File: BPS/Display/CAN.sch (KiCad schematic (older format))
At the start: 23 parts, among them J5 CAN_Out, U4 CDSOT23-T24CAN, U5 ADM3055E

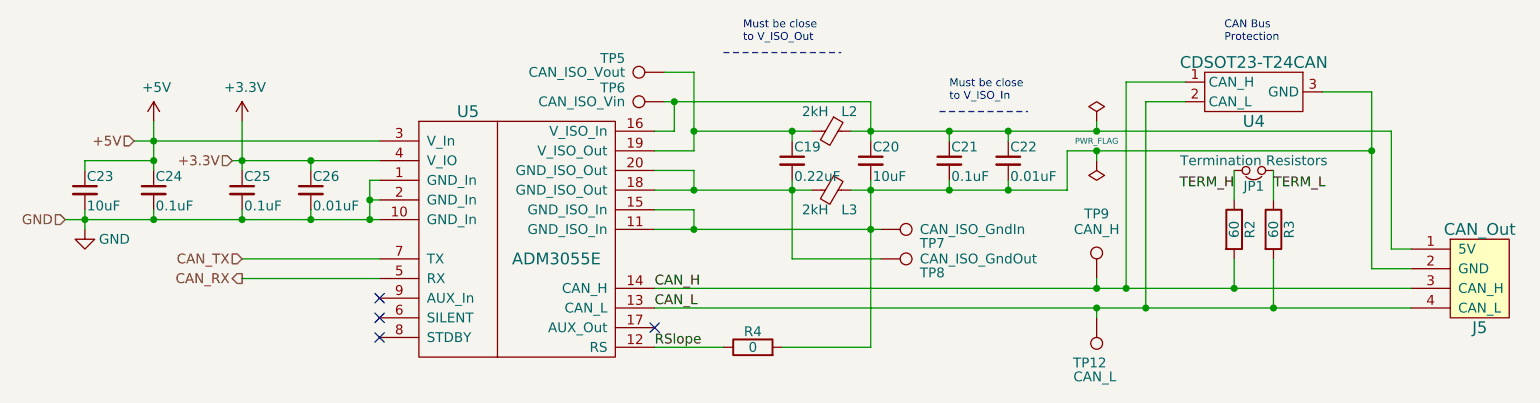
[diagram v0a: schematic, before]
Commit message: Creates schematics for display.
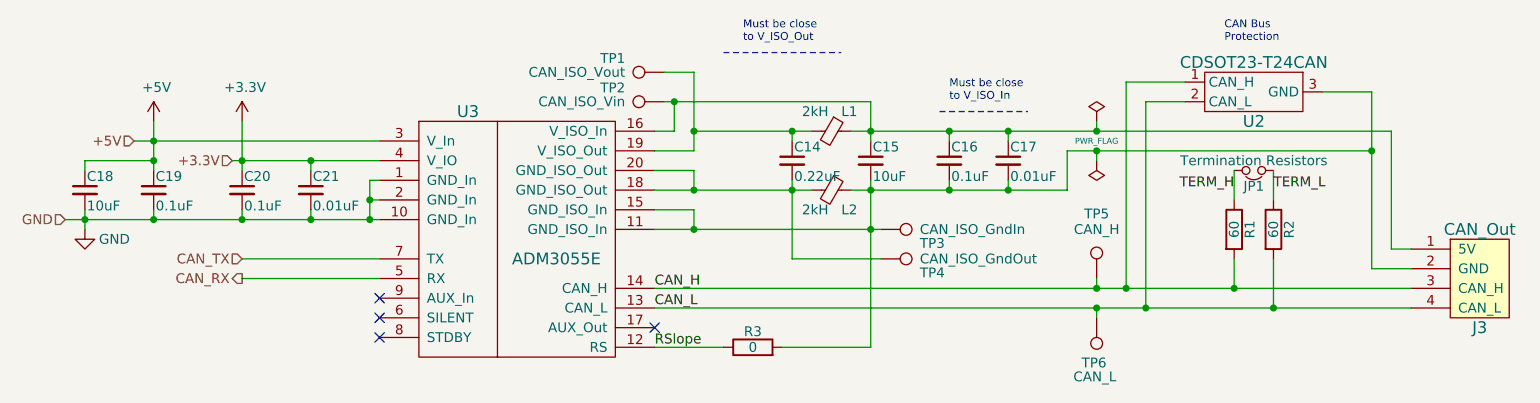
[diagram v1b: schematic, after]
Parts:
- renumbered C19 to C14, C20 to C15, C21 to C16, C22 to C17, C23 to C18, C24 to C19, C25 to C20, C26 to C21, J5 to J3, L2 to L1, L3 to L2, R2 to R1, R3 to R2, R4 to R3, TP5 to TP1, TP6 to TP2, TP7 to TP3, TP8 to TP4, TP9 to TP5, TP12 to TP6, U4 to U2, U5 to U3
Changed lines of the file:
@@
 EESchema Schematic File Version 4
-LIBS:BPSMaster-cache
+LIBS:BPSDisplay-cache
 EELAYER 29 0
 EELAYER END
 $Descr A4 11693 8268
 encoding utf-8
-Sheet 3 7
+Sheet 2 3
 Title ""
 Date ""
@@
 $EndDescr
 $Comp
-L utsvt-connectors:CANConnector J5
+L utsvt-connectors:CANConnector J3
 U 1 1 5C2B42F3
 P 9250 3800
-F 0 "J5" H 9250 3550 60  0000 C CNN
+F 0 "J3" H 9250 3550 60  0000 C CNN
 F 1 "CAN_Out" H 9250 4050 60  0000 C CNN
 F 2 "UTSVT_Connectors:Molex_MicroFit3.0_1x4xP3.00mm_PolarizingPeg_Vertical" H 9400 4100 60  0001 C CNN
@@
 $EndComp
 $Comp
-L Device:R R3
+L Device:R R2
 U 1 1 5C2B42FA
 P 8200 3550
-F 0 "R3" V 8280 3550 50  0000 C CNN
+F 0 "R2" V 8280 3550 50  0000 C CNN
 F 1 "60" V 8200 3550 50  0000 C CNN
 F 2 "Resistor_SMD:R_0805_2012Metric" V 8130 3550 50  0001 C CNN
@@
 $EndComp
 $Comp
-L Device:R R2
+L Device:R R1
 U 1 1 5C2B4301
 P 8000 3550
-F 0 "R2" V 8080 3550 50  0000 C CNN
+F 0 "R1" V 8080 3550 50  0000 C CNN
 F 1 "60" V 8000 3550 50  0000 C CNN
 F 2 "Resistor_SMD:R_0805_2012Metric" V 7930 3550 50  0001 C CNN
@@
 $EndComp
 $Comp
-L Device:C_Small C23
+L Device:C_Small C18
 U 1 1 5C2B4310
 P 2150 3350
-F 0 "C23" H 2160 3420 50  0000 L CNN
+F 0 "C18" H 2160 3420 50  0000 L CNN
 F 1 "10uF" H 2160 3270 50  0000 L CNN
 F 2 "Capacitor_SMD:C_0805_2012Metric" H 2150 3350 50  0001 C CNN
@@
 $EndComp
 $Comp
-L Device:C_Small C24
+L Device:C_Small C19
 U 1 1 5C2B4317
 P 2500 3350
-F 0 "C24" H 2510 3420 50  0000 L CNN
+F 0 "C19" H 2510 3420 50  0000 L CNN
 F 1 "0.1uF" H 2510 3270 50  0000 L CNN
 F 2 "Capacitor_SMD:C_0805_2012Metric" H 2500 3350 50  0001 C CNN
@@
 $EndComp
 $Comp
-L Device:C_Small C25
+L Device:C_Small C20
 U 1 1 5C2B431E
 P 2950 3350
-F 0 "C25" H 2960 3420 50  0000 L CNN
+F 0 "C20" H 2960 3420 50  0000 L CNN
 F 1 "0.1uF" H 2960 3270 50  0000 L CNN
 F 2 "Capacitor_SMD:C_0805_2012Metric" H 2950 3350 50  0001 C CNN
@@
 $EndComp
 $Comp
-L Device:C_Small C26
+L Device:C_Small C21
 U 1 1 5C2B4325
 P 3300 3350
-F 0 "C26" H 3310 3420 50  0000 L CNN
+F 0 "C21" H 3310 3420 50  0000 L CNN
 F 1 "0.01uF" H 3310 3270 50  0000 L CNN
 F 2 "Capacitor_SMD:C_0805_2012Metric" H 3300 3350 50  0001 C CNN
@@
 $EndComp
 $Comp
-L Device:C_Small C20
+L Device:C_Small C15
 U 1 1 5C2B432E
 P 6150 3200
-F 0 "C20" H 6160 3270 50  0000 L CNN
+F 0 "C15" H 6160 3270 50  0000 L CNN
 F 1 "10uF" H 6160 3120 50  0000 L CNN
 F 2 "Capacitor_SMD:C_0805_2012Metric" H 6150 3200 50  0001 C CNN
@@
 $EndComp
 $Comp
-L Device:C_Small C19
+L Device:C_Small C14
 U 1 1 5C2B4335
 P 5750 3200
-F 0 "C19" H 5760 3270 50  0000 L CNN
+F 0 "C14" H 5760 3270 50  0000 L CNN
 F 1 "0.22uF" H 5760 3120 50  0000 L CNN
 F 2 "Capacitor_SMD:C_0805_2012Metric" H 5750 3200 50  0001 C CNN
@@
 $EndComp
 $Comp
-L Device:Ferrite_Bead_Small L2
+L Device:Ferrite_Bead_Small L1
 U 1 1 5C2B433C
 P 5950 3050
-F 0 "L2" V 5850 3100 50  0000 L CNN
+F 0 "L1" V 5850 3100 50  0000 L CNN
 F 1 "2kH" V 5850 2900 50  0000 L CNN
 F 2 "Inductor_SMD:L_0805_2012Metric" V 5880 3050 50  0001 C CNN
@@
 $EndComp
 $Comp
-L Device:Ferrite_Bead_Small L3
+L Device:Ferrite_Bead_Small L2
 U 1 1 5C2B4343
 P 5950 3350
-F 0 "L3" V 6050 3400 50  0000 L CNN
+F 0 "L2" V 6050 3400 50  0000 L CNN
 F 1 "2kH" V 6050 3200 50  0000 L CNN
 F 2 "Inductor_SMD:L_0805_2012Metric" V 5880 3350 50  0001 C CNN
@@
 $EndComp
 $Comp
-L Device:C_Small C21
+L Device:C_Small C16
 U 1 1 5C2B434A
 P 6550 3200
-F 0 "C21" H 6560 3270 50  0000 L CNN
+F 0 "C16" H 6560 3270 50  0000 L CNN
 F 1 "0.1uF" H 6560 3120 50  0000 L CNN
 F 2 "Capacitor_SMD:C_0805_2012Metric" H 6550 3200 50  0001 C CNN
@@
 $EndComp
 $Comp
-L Device:C_Small C22
+L Device:C_Small C17
 U 1 1 5C2B4351
 P 6850 3200
-F 0 "C22" H 6860 3270 50  0000 L CNN
+F 0 "C17" H 6860 3270 50  0000 L CNN
 F 1 "0.01uF" H 6860 3120 50  0000 L CNN
 F 2 "Capacitor_SMD:C_0805_2012Metric" H 6850 3200 50  0001 C CNN
@@
 $EndComp
 $Comp
-L utsvt-chips:ADM3055E U5
+L utsvt-chips:ADM3055E U3
 U 1 1 5C2B4359
 P 4350 3600
-F 0 "U5" H 4100 4250 60  0000 C CNN
+F 0 "U3" H 4100 4250 60  0000 C CNN
 F 1 "ADM3055E" H 4550 3500 60  0000 C CNN
 F 2 "UTSVT_ICs:SOIC-20W_7.5x15.4mm_Pitch1.27mm" H 4350 3700 60  0001 C CNN
@@
 Must be close\nto V_ISO_In
 $Comp
-L Connector:TestPoint TP6
+L Connector:TestPoint TP2
 U 1 1 5C2B4371
 P 5100 2900
-F 0 "TP6" V 5200 3100 50  0000 L BNN
+F 0 "TP2" V 5200 3100 50  0000 L BNN
 F 1 "CAN_ISO_Vin" V 5100 3100 50  0000 L CNN
 F 2 "TestPoint:TestPoint_Keystone_5005-5009_Compact" H 5100 2900 50  0001 C CNN
@@
 $EndComp
 $Comp
-L Connector:TestPoint TP8
+L Connector:TestPoint TP4
 U 1 1 5C2B4378
 P 6200 3700
-F 0 "TP8" V 6300 3900 50  0000 L BNN
+F 0 "TP4" V 6300 3900 50  0000 L BNN
 F 1 "CAN_ISO_GndOut" V 6200 3900 50  0000 L CNN
 F 2 "TestPoint:TestPoint_Keystone_5005-5009_Compact" H 6200 3700 50  0001 C CNN
@@
 $EndComp
 $Comp
-L Connector:TestPoint TP7
+L Connector:TestPoint TP3
 U 1 1 5C2B437F
 P 6200 3550
-F 0 "TP7" V 6300 3750 50  0000 L BNN
+F 0 "TP3" V 6300 3750 50  0000 L BNN
 F 1 "CAN_ISO_GndIn" V 6200 3750 50  0000 L CNN
 F 2 "TestPoint:TestPoint_Keystone_5005-5009_Compact" H 6200 3550 50  0001 C CNN
@@
 $EndComp
 $Comp
-L Connector:TestPoint TP5
+L Connector:TestPoint TP1
 U 1 1 5C2B4386
 P 5100 2750
-F 0 "TP5" V 5200 2950 50  0000 L BNN
+F 0 "TP1" V 5200 2950 50  0000 L BNN
 F 1 "CAN_ISO_Vout" V 5100 2950 50  0000 L CNN
 F 2 "TestPoint:TestPoint_Keystone_5005-5009_Compact" H 5100 2750 50  0001 C CNN
@@
 NoConn ~ 3650 4100
 $Comp
-L power:PWR_FLAG #FLG03
+L power:PWR_FLAG #FLG0101
 U 1 1 5C2B4394
 P 7300 3000
-F 0 "#FLG03" H 7300 3075 50  0001 C CNN
+F 0 "#FLG0101" H 7300 3075 50  0001 C CNN
 F 1 "PWR_FLAG" H 7300 2900 30  0000 C CNN
 F 2 "" H 7300 3000 50  0001 C CNN
@@
 $EndComp
 $Comp
-L power:PWR_FLAG #FLG04
+L power:PWR_FLAG #FLG0102
 U 1 1 5C2B439A
 P 7300 3200
-F 0 "#FLG04" H 7300 3275 50  0001 C CNN
+F 0 "#FLG0102" H 7300 3275 50  0001 C CNN
 F 1 "PWR_FLAG" H 7200 3150 50  0001 L CNN
 F 2 "" H 7300 3200 50  0001 C CNN
@@
 $EndComp
 $Comp
-L utsvt-chips:CDSOT23-T24CAN U4
+L utsvt-chips:CDSOT23-T24CAN U2
 U 1 1 5C2B43A0
 P 8100 2850
-F 0 "U4" H 8100 2700 60  0000 C CNN
+F 0 "U2" H 8100 2700 60  0000 C CNN
 F 1 "CDSOT23-T24CAN" H 8100 3000 60  0000 C CNN
 F 2 "Package_TO_SOT_SMD:SOT-23W" H 8100 2850 60  0001 C CNN
@@
 CAN Bus\nProtection
 $Comp
-L Connector:TestPoint TP9
+L Connector:TestPoint TP5
 U 1 1 5C2B43B6
 P 7300 3800
-F 0 "TP9" H 7300 4100 50  0000 C BNN
+F 0 "TP5" H 7300 4100 50  0000 C BNN
 F 1 "CAN_H" H 7300 4050 50  0000 C CNN
 F 2 "TestPoint:TestPoint_Keystone_5005-5009_Compact" H 7300 3800 50  0001 C CNN
@@
 $EndComp
 $Comp
-L Connector:TestPoint TP12
+L Connector:TestPoint TP6
 U 1 1 5C2B43BD
 P 7300 4000
-F 0 "TP12" H 7250 4200 50  0000 L BNN
+F 0 "TP6" H 7250 4200 50  0000 L BNN
 F 1 "CAN_L" H 7200 4300 50  0000 L CNN
 F 2 "TestPoint:TestPoint_Keystone_5005-5009_Compact" H 7300 4000 50  0001 C CNN
@@
 $EndComp
 $Comp
-L Device:R R4
+L Device:R R3
 U 1 1 5C2B43C4
 P 5550 4150
-F 0 "R4" V 5630 4150 50  0000 C CNN
+F 0 "R3" V 5630 4150 50  0000 C CNN
 F 1 "0" V 5550 4150 50  0000 C CNN
 F 2 "Resistor_SMD:R_0805_2012Metric" V 5480 4150 50  0001 C CNN
@@
 	6150 3550 6200 3550
 $Comp
-L power:GND #PWR042
+L power:GND #PWR0118
 U 1 1 5C28BDDE
 P 2150 3550
-F 0 "#PWR042" H 2150 3300 50  0001 C CNN
+F 0 "#PWR0118" H 2150 3300 50  0001 C CNN
 F 1 "GND" H 2300 3500 50  0000 C CNN
 F 2 "" H 2150 3550 50  0001 C CNN
@@
 	2500 3000 2500 3100
 $Comp
-L power:+3.3V #PWR0133
+L power:+3.3V #PWR0119
 U 1 1 5C4ABE05
 P 2950 3000
-F 0 "#PWR0133" H 2950 2850 50  0001 C CNN
+F 0 "#PWR0119" H 2950 2850 50  0001 C CNN
 F 1 "+3.3V" H 2965 3173 50  0000 C CNN
 F 2 "" H 2950 3000 50  0001 C CNN
@@
 	2950 3000 2950 3200
 $Comp
-L power:+5V #PWR0132
+L power:+5V #PWR0120
 U 1 1 5C4C2AB0
 P 2500 3000
-F 0 "#PWR0132" H 2500 2850 50  0001 C CNN
+F 0 "#PWR0120" H 2500 2850 50  0001 C CNN
 F 1 "+5V" H 2515 3173 50  0000 C CNN
 F 2 "" H 2500 3000 50  0001 C CNN

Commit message: Display, Board Layout
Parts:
- J3: footprint UTSVT_Connectors:Molex_MicroFit3.0_1x4xP3.00mm_PolarizingPeg_Vertical -> Connector_Molex:Molex_Micro-Fit_3.0_43650-0400_1x04_P3.00mm_Horizontal; symbol utsvt-connectors:CANConnector -> BPSDisplay-rescue:CANConnector-utsvt-connectors
- U2: symbol utsvt-chips:CDSOT23-T24CAN -> BPSDisplay-rescue:CDSOT23-T24CAN-utsvt-chips
- U3: symbol utsvt-chips:ADM3055E -> BPSDisplay-rescue:ADM3055E-utsvt-chips
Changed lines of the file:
@@
 $EndDescr
 $Comp
-L utsvt-connectors:CANConnector J3
+L BPSDisplay-rescue:CANConnector-utsvt-connectors J3
 U 1 1 5C2B42F3
 P 9250 3800
 F 0 "J3" H 9250 3550 60  0000 C CNN
 F 1 "CAN_Out" H 9250 4050 60  0000 C CNN
-F 2 "UTSVT_Connectors:Molex_MicroFit3.0_1x4xP3.00mm_PolarizingPeg_Vertical" H 9400 4100 60  0001 C CNN
+F 2 "Connector_Molex:Molex_Micro-Fit_3.0_43650-0400_1x04_P3.00mm_Horizontal" H 9400 4100 60  0001 C CNN
 F 3 "" H 9400 4100 60  0001 C CNN
 	1    9250 3800
@@
 $EndComp
 $Comp
-L utsvt-chips:ADM3055E U3
+L BPSDisplay-rescue:ADM3055E-utsvt-chips U3
 U 1 1 5C2B4359
 P 4350 3600
@@
 $EndComp
 $Comp
-L utsvt-chips:CDSOT23-T24CAN U2
+L BPSDisplay-rescue:CDSOT23-T24CAN-utsvt-chips U2
 U 1 1 5C2B43A0
 P 8100 2850

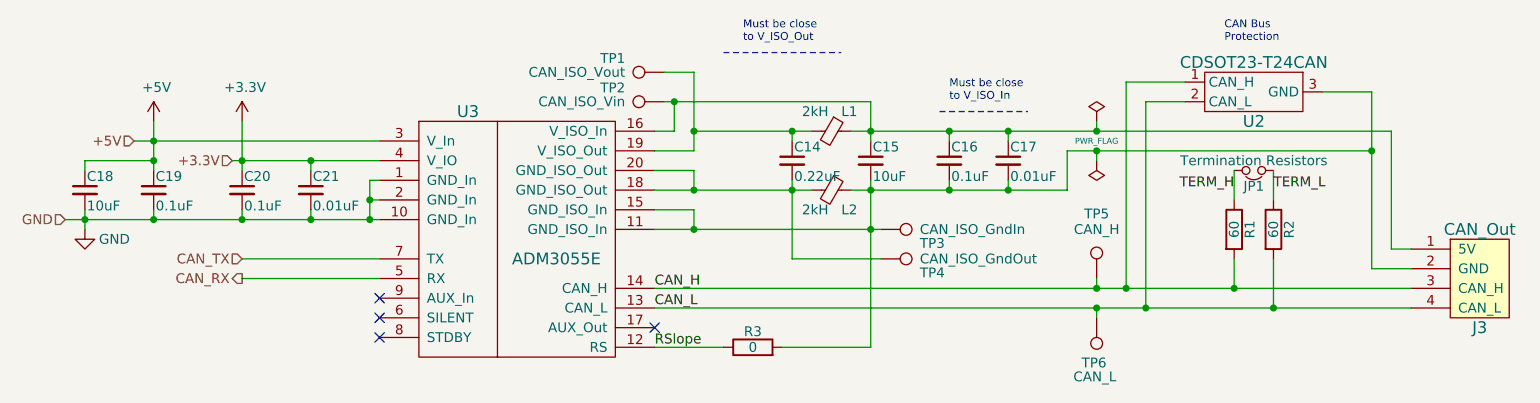
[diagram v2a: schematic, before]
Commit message: Adds display board
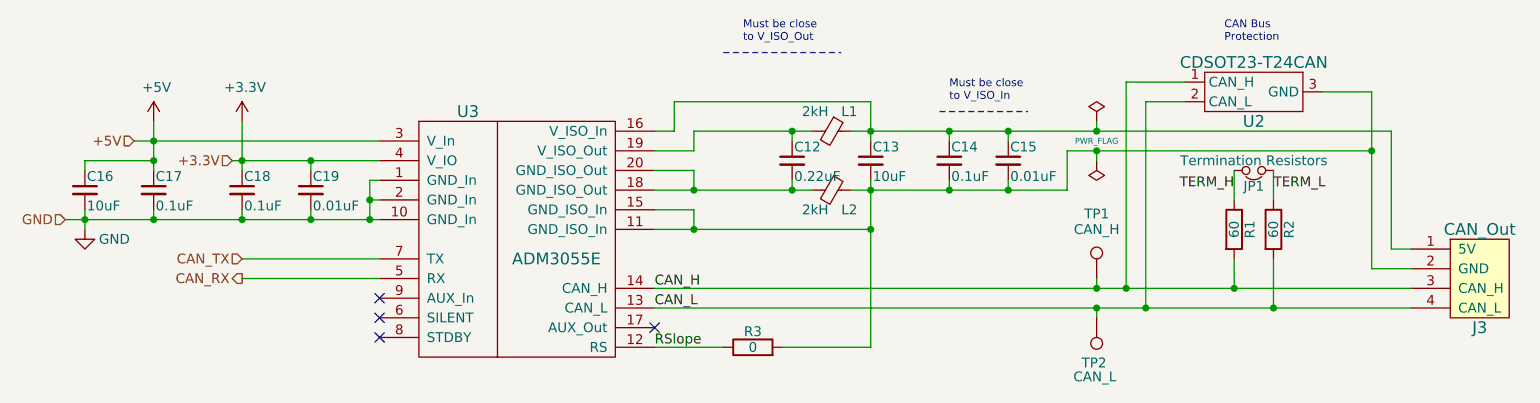
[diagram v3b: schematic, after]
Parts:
- removed TP1: CAN_ISO_Vout, TestPoint:TestPoint_Keystone_5005-5009_Compact, symbol Connector:TestPoint
- removed TP2: CAN_ISO_Vin, TestPoint:TestPoint_Keystone_5005-5009_Compact, symbol Connector:TestPoint
- removed TP3: CAN_ISO_GndIn, TestPoint:TestPoint_Keystone_5005-5009_Compact, symbol Connector:TestPoint
- removed TP4: CAN_ISO_GndOut, TestPoint:TestPoint_Keystone_5005-5009_Compact, symbol Connector:TestPoint
- renumbered C14 to C12, C15 to C13, C16 to C14, C17 to C15, C18 to C16, C19 to C17, C20 to C18, C21 to C19, TP5 to TP1, TP6 to TP2
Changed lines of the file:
@@
 EESchema Schematic File Version 4
-LIBS:BPSDisplay-cache
-EELAYER 29 0
+EELAYER 30 0
 EELAYER END
 $Descr A4 11693 8268
 encoding utf-8
-Sheet 2 3
+Sheet 2 4
 Title ""
 Date ""
@@
 $EndComp
 $Comp
-L Device:C_Small C18
+L Device:C_Small C16
 U 1 1 5C2B4310
 P 2150 3350
-F 0 "C18" H 2160 3420 50  0000 L CNN
+F 0 "C16" H 2160 3420 50  0000 L CNN
 F 1 "10uF" H 2160 3270 50  0000 L CNN
 F 2 "Capacitor_SMD:C_0805_2012Metric" H 2150 3350 50  0001 C CNN
@@
 $EndComp
 $Comp
-L Device:C_Small C19
+L Device:C_Small C17
 U 1 1 5C2B4317
 P 2500 3350
-F 0 "C19" H 2510 3420 50  0000 L CNN
+F 0 "C17" H 2510 3420 50  0000 L CNN
 F 1 "0.1uF" H 2510 3270 50  0000 L CNN
 F 2 "Capacitor_SMD:C_0805_2012Metric" H 2500 3350 50  0001 C CNN
@@
 $EndComp
 $Comp
-L Device:C_Small C20
+L Device:C_Small C18
 U 1 1 5C2B431E
 P 2950 3350
-F 0 "C20" H 2960 3420 50  0000 L CNN
+F 0 "C18" H 2960 3420 50  0000 L CNN
 F 1 "0.1uF" H 2960 3270 50  0000 L CNN
 F 2 "Capacitor_SMD:C_0805_2012Metric" H 2950 3350 50  0001 C CNN
@@
 $EndComp
 $Comp
-L Device:C_Small C21
+L Device:C_Small C19
 U 1 1 5C2B4325
 P 3300 3350
-F 0 "C21" H 3310 3420 50  0000 L CNN
+F 0 "C19" H 3310 3420 50  0000 L CNN
 F 1 "0.01uF" H 3310 3270 50  0000 L CNN
 F 2 "Capacitor_SMD:C_0805_2012Metric" H 3300 3350 50  0001 C CNN
@@
 $EndComp
 $Comp
-L Device:C_Small C15
+L Device:C_Small C13
 U 1 1 5C2B432E
 P 6150 3200
-F 0 "C15" H 6160 3270 50  0000 L CNN
+F 0 "C13" H 6160 3270 50  0000 L CNN
 F 1 "10uF" H 6160 3120 50  0000 L CNN
 F 2 "Capacitor_SMD:C_0805_2012Metric" H 6150 3200 50  0001 C CNN
@@
 $EndComp
 $Comp
-L Device:C_Small C14
+L Device:C_Small C12
 U 1 1 5C2B4335
 P 5750 3200
-F 0 "C14" H 5760 3270 50  0000 L CNN
+F 0 "C12" H 5760 3270 50  0000 L CNN
 F 1 "0.22uF" H 5760 3120 50  0000 L CNN
 F 2 "Capacitor_SMD:C_0805_2012Metric" H 5750 3200 50  0001 C CNN
@@
 $EndComp
 $Comp
-L Device:C_Small C16
+L Device:C_Small C14
 U 1 1 5C2B434A
 P 6550 3200
-F 0 "C16" H 6560 3270 50  0000 L CNN
+F 0 "C14" H 6560 3270 50  0000 L CNN
 F 1 "0.1uF" H 6560 3120 50  0000 L CNN
 F 2 "Capacitor_SMD:C_0805_2012Metric" H 6550 3200 50  0001 C CNN
@@
 $EndComp
 $Comp
-L Device:C_Small C17
+L Device:C_Small C15
 U 1 1 5C2B4351
 P 6850 3200
-F 0 "C17" H 6860 3270 50  0000 L CNN
+F 0 "C15" H 6860 3270 50  0000 L CNN
 F 1 "0.01uF" H 6860 3120 50  0000 L CNN
 F 2 "Capacitor_SMD:C_0805_2012Metric" H 6850 3200 50  0001 C CNN
@@
 Text Notes 6550 2900 0    40   ~ 0
 Must be close\nto V_ISO_In
-$Comp
-L Connector:TestPoint TP2
-U 1 1 5C2B4371
-P 5100 2900
-F 0 "TP2" V 5200 3100 50  0000 L BNN
-F 1 "CAN_ISO_Vin" V 5100 3100 50  0000 L CNN
-F 2 "TestPoint:TestPoint_Keystone_5005-5009_Compact" H 5100 2900 50  0001 C CNN
-F 3 "" H 5100 2900 50  0001 C CNN
-	1    5100 2900
-	0    -1   -1   0
-$EndComp
-$Comp
-L Connector:TestPoint TP4
-U 1 1 5C2B4378
-P 6200 3700
-F 0 "TP4" V 6300 3900 50  0000 L BNN
-F 1 "CAN_ISO_GndOut" V 6200 3900 50  0000 L CNN
-F 2 "TestPoint:TestPoint_Keystone_5005-5009_Compact" H 6200 3700 50  0001 C CNN
-F 3 "" H 6200 3700 50  0001 C CNN
-	1    6200 3700
-	0    1    1    0
-$EndComp
-$Comp
-L Connector:TestPoint TP3
-U 1 1 5C2B437F
-P 6200 3550
-F 0 "TP3" V 6300 3750 50  0000 L BNN
-F 1 "CAN_ISO_GndIn" V 6200 3750 50  0000 L CNN
-F 2 "TestPoint:TestPoint_Keystone_5005-5009_Compact" H 6200 3550 50  0001 C CNN
-F 3 "" H 6200 3550 50  0001 C CNN
-	1    6200 3550
-	0    1    1    0
-$EndComp
-$Comp
-L Connector:TestPoint TP1
-U 1 1 5C2B4386
-P 5100 2750
-F 0 "TP1" V 5200 2950 50  0000 L BNN
-F 1 "CAN_ISO_Vout" V 5100 2950 50  0000 L CNN
-F 2 "TestPoint:TestPoint_Keystone_5005-5009_Compact" H 5100 2750 50  0001 C CNN
-F 3 "" H 5100 2750 50  0001 C CNN
-	1    5100 2750
-	0    -1   -1   0
-$EndComp
 NoConn ~ 3650 4100
 $Comp
-L power:PWR_FLAG #FLG0101
+L power:PWR_FLAG #FLG01
 U 1 1 5C2B4394
 P 7300 3000
-F 0 "#FLG0101" H 7300 3075 50  0001 C CNN
+F 0 "#FLG01" H 7300 3075 50  0001 C CNN
 F 1 "PWR_FLAG" H 7300 2900 30  0000 C CNN
 F 2 "" H 7300 3000 50  0001 C CNN
@@
 $EndComp
 $Comp
-L power:PWR_FLAG #FLG0102
+L power:PWR_FLAG #FLG02
 U 1 1 5C2B439A
 P 7300 3200
-F 0 "#FLG0102" H 7300 3275 50  0001 C CNN
+F 0 "#FLG02" H 7300 3275 50  0001 C CNN
 F 1 "PWR_FLAG" H 7200 3150 50  0001 L CNN
 F 2 "" H 7300 3200 50  0001 C CNN
@@
 CAN Bus\nProtection
 $Comp
-L Connector:TestPoint TP5
+L Connector:TestPoint TP1
 U 1 1 5C2B43B6
 P 7300 3800
-F 0 "TP5" H 7300 4100 50  0000 C BNN
+F 0 "TP1" H 7300 4100 50  0000 C BNN
 F 1 "CAN_H" H 7300 4050 50  0000 C CNN
 F 2 "TestPoint:TestPoint_Keystone_5005-5009_Compact" H 7300 3800 50  0001 C CNN
@@
 $EndComp
 $Comp
-L Connector:TestPoint TP6
+L Connector:TestPoint TP2
 U 1 1 5C2B43BD
 P 7300 4000
-F 0 "TP6" H 7250 4200 50  0000 L BNN
+F 0 "TP2" H 7250 4200 50  0000 L BNN
 F 1 "CAN_L" H 7200 4300 50  0000 L CNN
 F 2 "TestPoint:TestPoint_Keystone_5005-5009_Compact" H 7300 4000 50  0001 C CNN
@@
 	5250 3150 5050 3150
 Wire Wire Line
-	5100 2900 5150 2900
-Wire Wire Line
 	5150 2900 5150 3050
 Wire Wire Line
@@
 Wire Wire Line
 	8200 3250 8200 3400
-Connection ~ 5150 2900
 Connection ~ 5250 3350
 Connection ~ 6150 3550
 Wire Wire Line
-	5100 2750 5250 2750
-Wire Wire Line
 	7300 3200 7300 3150
 Wire Wire Line
@@
 Wire Wire Line
 	5250 3050 5250 3150
-Wire Wire Line
-	5750 3350 5750 3700
-Wire Wire Line
-	6150 3550 6200 3550
-$Comp
-L power:GND #PWR0118
+$Comp
+L power:GND #PWR028
 U 1 1 5C28BDDE
 P 2150 3550
-F 0 "#PWR0118" H 2150 3300 50  0001 C CNN
+F 0 "#PWR028" H 2150 3300 50  0001 C CNN
 F 1 "GND" H 2300 3500 50  0000 C CNN
 F 2 "" H 2150 3550 50  0001 C CNN
@@
 	7300 3950 7550 3950
 Connection ~ 5750 3350
-Wire Wire Line
-	5250 3350 5750 3350
-Wire Wire Line
-	5750 3700 6200 3700
 Text Label 5050 3850 0    50   ~ 0
 CAN_H
@@
 Wire Wire Line
 	5250 3050 5750 3050
-Connection ~ 5250 3050
-Wire Wire Line
-	5150 2900 5250 2900
-Wire Wire Line
-	5250 2900 6150 2900
-Wire Wire Line
-	5250 2750 5250 3050
 Text Label 5050 4150 0    50   ~ 0
 RSlope
@@
 	2500 3000 2500 3100
 $Comp
-L power:+3.3V #PWR0119
+L power:+3.3V #PWR027
 U 1 1 5C4ABE05
 P 2950 3000
-F 0 "#PWR0119" H 2950 2850 50  0001 C CNN
+F 0 "#PWR027" H 2950 2850 50  0001 C CNN
 F 1 "+3.3V" H 2965 3173 50  0000 C CNN
 F 2 "" H 2950 3000 50  0001 C CNN
@@
 	2950 3000 2950 3200
 $Comp
-L power:+5V #PWR0120
+L power:+5V #PWR026
 U 1 1 5C4C2AB0
 P 2500 3000
-F 0 "#PWR0120" H 2500 2850 50  0001 C CNN
+F 0 "#PWR026" H 2500 2850 50  0001 C CNN
 F 1 "+5V" H 2515 3173 50  0000 C CNN
 F 2 "" H 2500 3000 50  0001 C CNN
@@
 Wire Wire Line
 	2950 3800 3650 3800
+Wire Wire Line
+	5150 2900 6150 2900
+Wire Wire Line
+	5250 3350 5750 3350
 $EndSCHEMATC
